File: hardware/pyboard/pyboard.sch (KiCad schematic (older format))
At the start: 66 parts, among them J1 Battery, J10 P9-P10, J2 Y1-Y8, J3 X9-X16, J4 USB_B_Micro, J5 P1-P8, J6 X17-X24, J7 Y9-Y16, J8 X1-X8, J9 Micro_SD_Card_Det, Q1 DMP2165UW, SW1 RST, SW2 USR, U1 STM32F405RGT6, U2 MCP1703A-3302_SOT89, U3 MIC2005A-1YM5, U4 MMA7660FC, Y1 32.768kHz, Y2 12MHz

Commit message: Fix ERC errors
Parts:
- C1, C10, C11, C12, C13, C14, C15, C16, C17, C18, C19, C2, C3, C4, C5, C6, C7, C8, C9: footprint (none) -> Capacitor_SMD:C_0603_1608Metric
- C20: value C -> 4.7uF; footprint (none) -> Capacitor_SMD:C_0603_1608Metric
- D1: footprint (none) -> Diode_SMD:D_SOD-123F
- R1, R10, R11, R12, R13, R14, R15, R16, R17, R18, R19, R2, R20, R21, R3, R4, R5, R6, R7, R8, R9: footprint (none) -> Resistor_SMD:R_0603_1608Metric
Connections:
- net labels removed: +BATT, SIDO_CK
- wire segments 341 -> 338
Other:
- moved on the sheet: D1, J1, R16

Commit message: Add footprint for LED
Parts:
- D2, D3, D4, D5: footprint (none) -> LED_SMD:LED_1206_3216Metric
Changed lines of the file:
@@
 F 0 "D5" H 14793 8816 50  0000 C CNN
 F 1 "LED_BLUE" H 14793 8725 50  0000 C CNN
-F 2 "" H 14800 8600 50  0001 C CNN
+F 2 "LED_SMD:LED_1206_3216Metric" H 14800 8600 50  0001 C CNN
 F 3 "~" H 14800 8600 50  0001 C CNN
 	1    14800 8600
@@
 F 0 "D4" H 14793 8466 50  0000 C CNN
 F 1 "LED_YELLOW" H 14793 8375 50  0000 C CNN
-F 2 "" H 14800 8250 50  0001 C CNN
+F 2 "LED_SMD:LED_1206_3216Metric" H 14800 8250 50  0001 C CNN
 F 3 "~" H 14800 8250 50  0001 C CNN
 	1    14800 8250
@@
 F 0 "D3" H 14793 8116 50  0000 C CNN
 F 1 "LED_GREEN" H 14793 8025 50  0000 C CNN
-F 2 "" H 14800 7900 50  0001 C CNN
+F 2 "LED_SMD:LED_1206_3216Metric" H 14800 7900 50  0001 C CNN
 F 3 "~" H 14800 7900 50  0001 C CNN
 	1    14800 7900
@@
 F 0 "D2" H 14793 7766 50  0000 C CNN
 F 1 "LED_RED" H 14793 7675 50  0000 C CNN
-F 2 "" H 14800 7550 50  0001 C CNN
+F 2 "LED_SMD:LED_1206_3216Metric" H 14800 7550 50  0001 C CNN
 F 3 "~" H 14800 7550 50  0001 C CNN
 	1    14800 7550

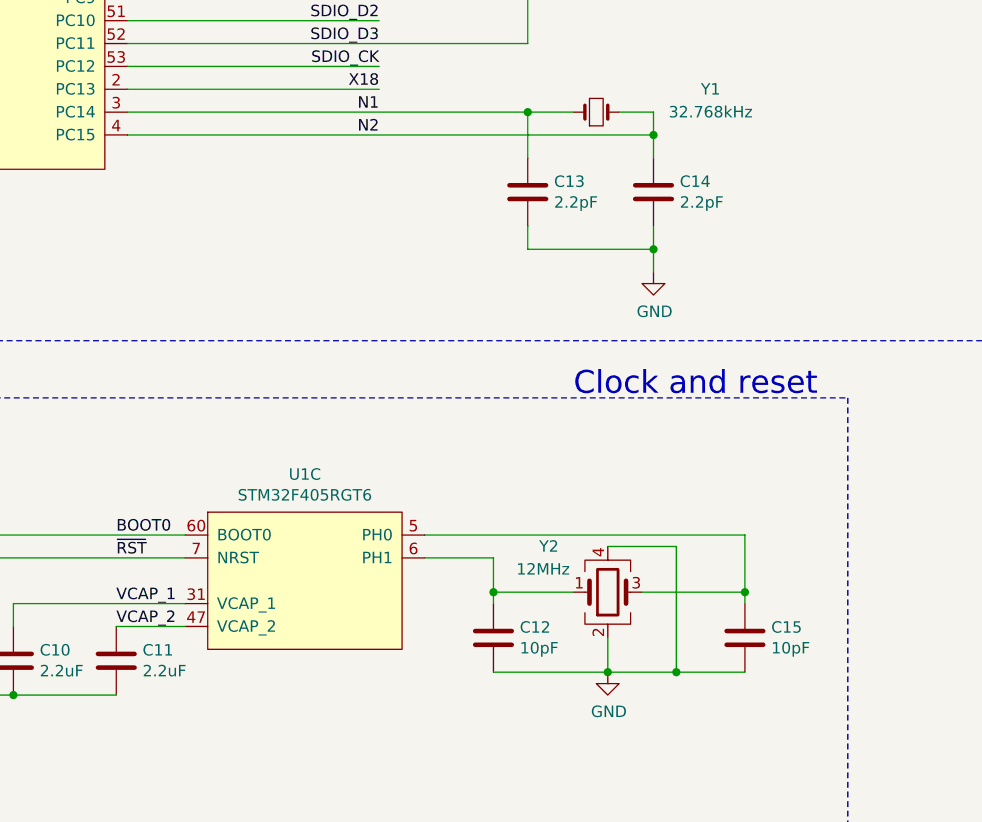
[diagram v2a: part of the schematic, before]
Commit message: Add footprints for ICs
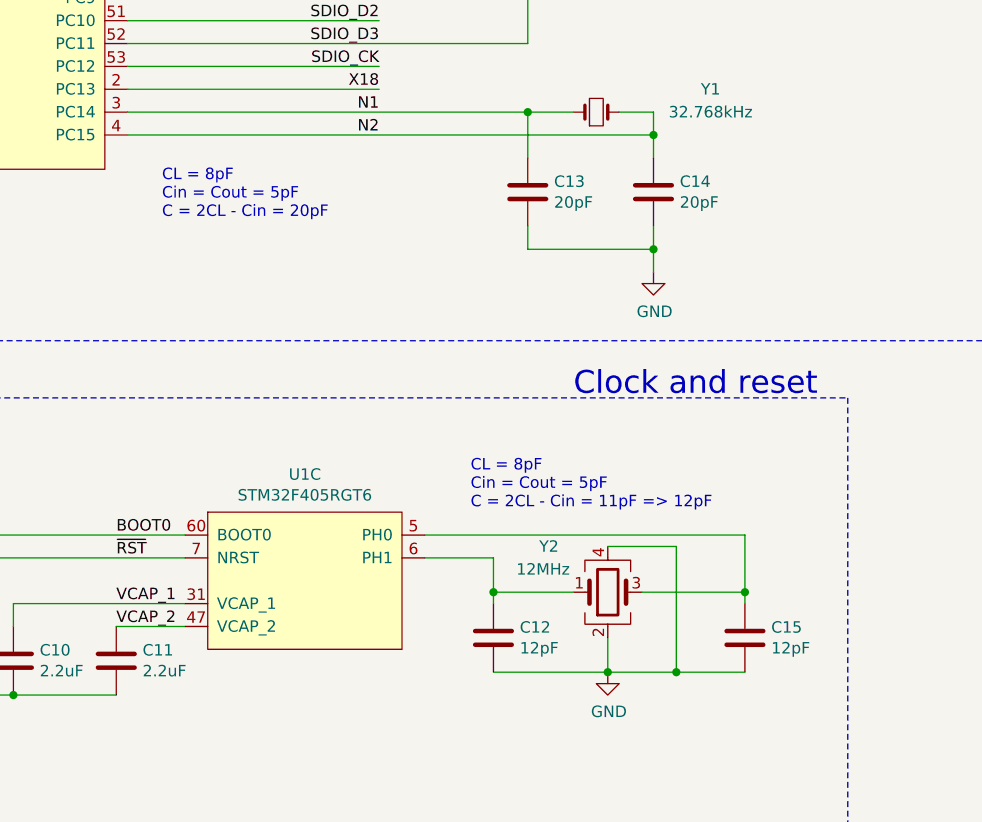
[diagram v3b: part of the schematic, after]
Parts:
- C12, C15: value 10pF -> 12pF
- C13, C14: value 2.2pF -> 20pF
- FB1: footprint (none) -> Resistor_SMD:R_0603_1608Metric
- U1: footprint (none) -> Package_QFP:LQFP-64_10x10mm_P0.5mm
- U4: footprint (none) -> components:DFN-10_3x3mm
- Y1: footprint (none) -> Crystal:Crystal_SMD_3215-2Pin_3.2x1.5mm
- Y2: footprint (none) -> Crystal:Crystal_SMD_3225-4Pin_3.2x2.5mm
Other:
- note added: "CL = 8pF\nCin = Cout = 5pF\nC = 2CL - Cin = 11pF => 12pF\n"
- note added: "CL = 8pF\nCin = Cout = 5pF\nC = 2CL - Cin = 20pF\n"

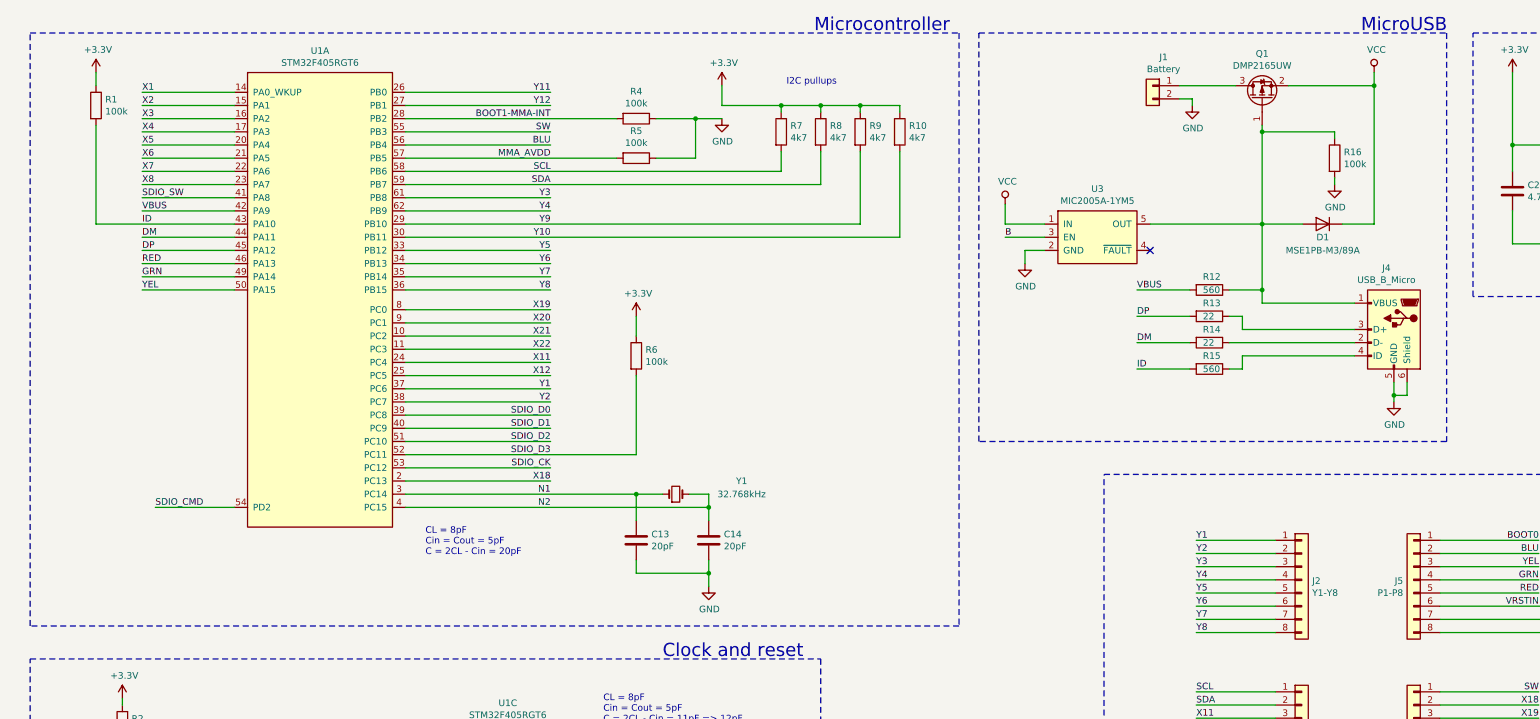
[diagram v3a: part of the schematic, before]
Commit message: Change power switch model
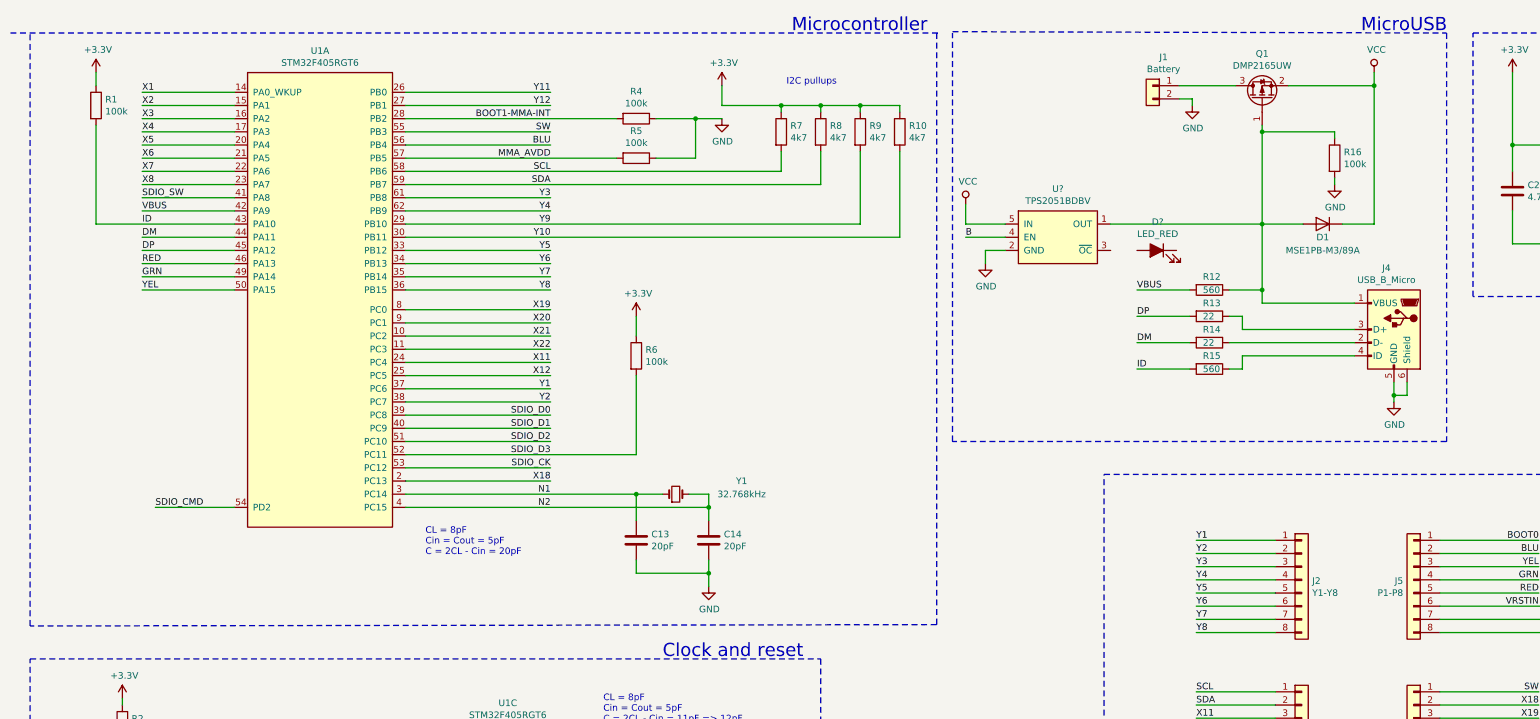
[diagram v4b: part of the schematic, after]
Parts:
- removed U3: MIC2005A-1YM5, symbol components:MIC2005A-1YM5
- added D?: LED_RED, LED_SMD:LED_1206_3216Metric, symbol Device:LED_ALT
- added U?: TPS2051BDBV, symbol components:TPS2051BDBV
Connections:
- no-connect marks 5 -> 4
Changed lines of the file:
@@
 L power:VCC #PWR019
 U 1 1 5D9373D3
-P 8400 2050
-F 0 "#PWR019" H 8400 1900 50  0001 C CNN
-F 1 "VCC" H 8417 2223 50  0000 C CNN
-F 2 "" H 8400 2050 50  0001 C CNN
-F 3 "" H 8400 2050 50  0001 C CNN
-	1    8400 2050
-	1    0    0    -1
-$EndComp
-Text Label 8400 2300 0    50   ~ 0
+P 8100 2050
+F 0 "#PWR019" H 8100 1900 50  0001 C CNN
+F 1 "VCC" H 8117 2223 50  0000 C CNN
+F 2 "" H 8100 2050 50  0001 C CNN
+F 3 "" H 8100 2050 50  0001 C CNN
+	1    8100 2050
+	1    0    0    -1
+$EndComp
+Text Label 8100 2300 0    50   ~ 0
 B
 $Comp
 L power:GND #PWR020
 U 1 1 5D9470BD
-P 8550 2500
-F 0 "#PWR020" H 8550 2250 50  0001 C CNN
-F 1 "GND" H 8555 2327 50  0000 C CNN
-F 2 "" H 8550 2500 50  0001 C CNN
-F 3 "" H 8550 2500 50  0001 C CNN
-	1    8550 2500
-	1    0    0    -1
-$EndComp
-Wire Wire Line
-	8550 2400 8550 2500
+P 8250 2500
+F 0 "#PWR020" H 8250 2250 50  0001 C CNN
+F 1 "GND" H 8255 2327 50  0000 C CNN
+F 2 "" H 8250 2500 50  0001 C CNN
+F 3 "" H 8250 2500 50  0001 C CNN
+	1    8250 2500
+	1    0    0    -1
+$EndComp
+Wire Wire Line
+	8250 2400 8250 2500
 $Comp
 L power:VCC #PWR031
@@
 	1    0    0    -1
 $EndComp
-NoConn ~ 9500 2400
-Wire Wire Line
-	8400 2300 8700 2300
-Wire Wire Line
-	8700 2400 8550 2400
-Wire Wire Line
-	8400 2200 8700 2200
-Wire Wire Line
-	9500 2200 10350 2200
+Wire Wire Line
+	8100 2300 8400 2300
+Wire Wire Line
+	8400 2400 8250 2400
+Wire Wire Line
+	8100 2200 8400 2200
 Wire Wire Line
 	10900 1900 10900 1850
@@
 	1000 5500 7000 5500
 Wire Notes Line
-	8050 5250 1000 5250
-Wire Notes Line
-	8050 750  8050 5250
-Wire Notes Line
-	1000 750  8050 750
+	7880 5240 1000 5250
+Wire Notes Line
+	7880 750  7880 5250
+Wire Notes Line
+	850  750  7900 750
 Wire Notes Line
 	1000 5250 1000 750
@@
 Wire Notes Line
 	1000 8000 5500 8000
-Text Notes 6950 750  0    100  ~ 0
+Text Notes 6780 750  0    100  ~ 0
 Microcontroller
 Text Notes 4500 8000 0    100  ~ 0
@@
 MicroSD
 Wire Notes Line
-	8200 750  11750 750
+	8000 740  11750 750
 Wire Notes Line
 	11750 750  11750 3850
 Wire Notes Line
-	11750 3850 8200 3850
-Wire Notes Line
-	8200 3850 8200 750
+	11750 3850 8000 3850
+Wire Notes Line
+	8000 3850 8000 750
 Text Notes 11100 750  0    100  ~ 0
 MicroUSB
@@
 	11200 1050 11200 1150
 Wire Wire Line
-	8400 2050 8400 2200
+	8100 2050 8100 2200
 Wire Wire Line
 	14150 4450 14150 4600
@@
 $EndComp
 $Comp
-L components:MIC2005A-1YM5 U3
-U 1 1 5D812FDB
-P 9100 2300
-F 0 "U3" H 9100 2667 50  0000 C CNN
-F 1 "MIC2005A-1YM5" H 9100 2576 50  0000 C CNN
-F 2 "" H 9100 2300 50  0001 C CNN
-F 3 "http://ww1.microchip.com/downloads/en/DeviceDoc/mic20xx.pdf" H 9100 2300 50  0001 C CNN
-	1    9100 2300
-	1    0    0    -1
-$EndComp
-$Comp
 L Device:R R16
 U 1 1 5D983925
@@
 Text Notes 4000 4720 0    50   ~ 0
 CL = 8pF\nCin = Cout = 5pF\nC = 2CL - Cin = 20pF\n
+$Comp
+L components:TPS2051BDBV U?
+U 1 1 5D9F4D8D
+P 8800 2300
+F 0 "U?" H 8800 2667 50  0000 C CNN
+F 1 "TPS2051BDBV" H 8800 2576 50  0000 C CNN
+F 2 "" H 8800 2300 50  0001 C CNN
+F 3 "" H 8800 2300 50  0001 C CNN
+	1    8800 2300
+	1    0    0    -1
+$EndComp
+$Comp
+L Device:LED_ALT D?
+U 1 1 5D9F5F29
+P 9550 2400
+F 0 "D?" H 9543 2616 50  0000 C CNN
+F 1 "LED_RED" H 9543 2525 50  0000 C CNN
+F 2 "LED_SMD:LED_1206_3216Metric" H 9550 2400 50  0001 C CNN
+F 3 "~" H 9550 2400 50  0001 C CNN
+	1    9550 2400
+	-1   0    0    -1
+$EndComp
+Wire Wire Line
+	9200 2200 10350 2200
 $EndSCHEMATC

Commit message: WIP: add mosfet and led
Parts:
- removed D?: LED_RED, LED_SMD:LED_1206_3216Metric, symbol Device:LED_ALT
- added D?: LED_ALT, symbol Device:LED_ALT
- added Q?: IRLML6402, Package_TO_SOT_SMD:SOT-23, symbol Transistor_FET:IRLML6402
- added R?: 110, symbol Device:R
- added R?: 4k7, symbol Device:R
- added R?: 560, Resistor_SMD:R_0603_1608Metric, symbol Device:R
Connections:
- wire segments 338 -> 350
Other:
- moved on the sheet: C1, C10, C11, C12, C13, C14, C15, C16, C17, C2, C20, C3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

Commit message: Move overcurrent block
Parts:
- removed D1: MSE1PB-M3/89A, Diode_SMD:D_SOD-123F, symbol Device:D
- removed D?: LED_ALT, symbol Device:LED_ALT
- removed Q?: IRLML6402, Package_TO_SOT_SMD:SOT-23, symbol Transistor_FET:IRLML6402
- removed R?: 110, symbol Device:R
- removed U?: TPS2051BDBV, symbol components:TPS2051BDBV
- added D1: OC_RED, LED_SMD:LED_1206_3216Metric, symbol Device:LED_ALT
- added D6: MSE1PB-M3/89A, Diode_SMD:D_SOD-123F, symbol Device:D
- added Q2: IRLML6402, Package_TO_SOT_SMD:SOT-23, symbol Transistor_FET:IRLML6402
- added R24: 110, symbol Device:R
- added U3: TPS2051BDBV, Package_TO_SOT_SMD:SOT-23-5, symbol components:TPS2051BDBV
- gave numbers to parts that had none: 2
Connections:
- net labels added: ~OC
- wire segments 350 -> 349
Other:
- moved on the sheet: C20, J4, J9, Q1, R11, R12, R13, R14, R15, R16, R22, R23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
